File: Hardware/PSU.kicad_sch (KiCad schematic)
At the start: 6 parts, among them J2 Power, U3 HT7533

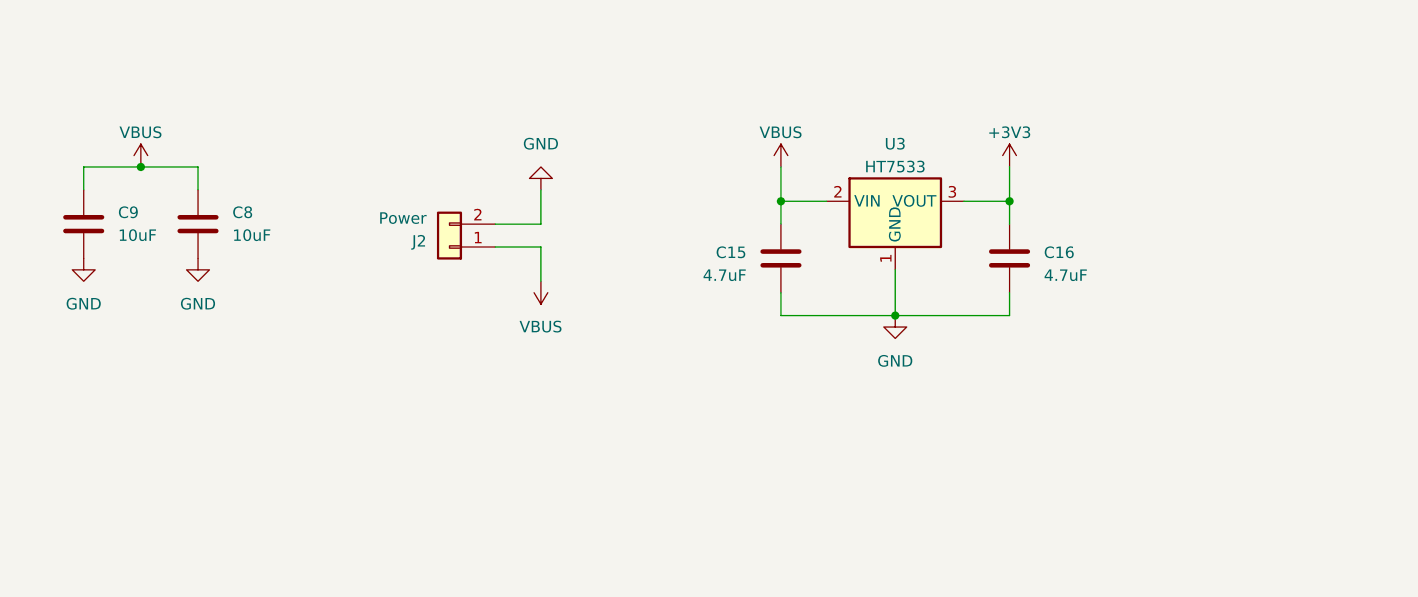
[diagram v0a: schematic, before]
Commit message: 完成原理图设计，完成初步布局布线
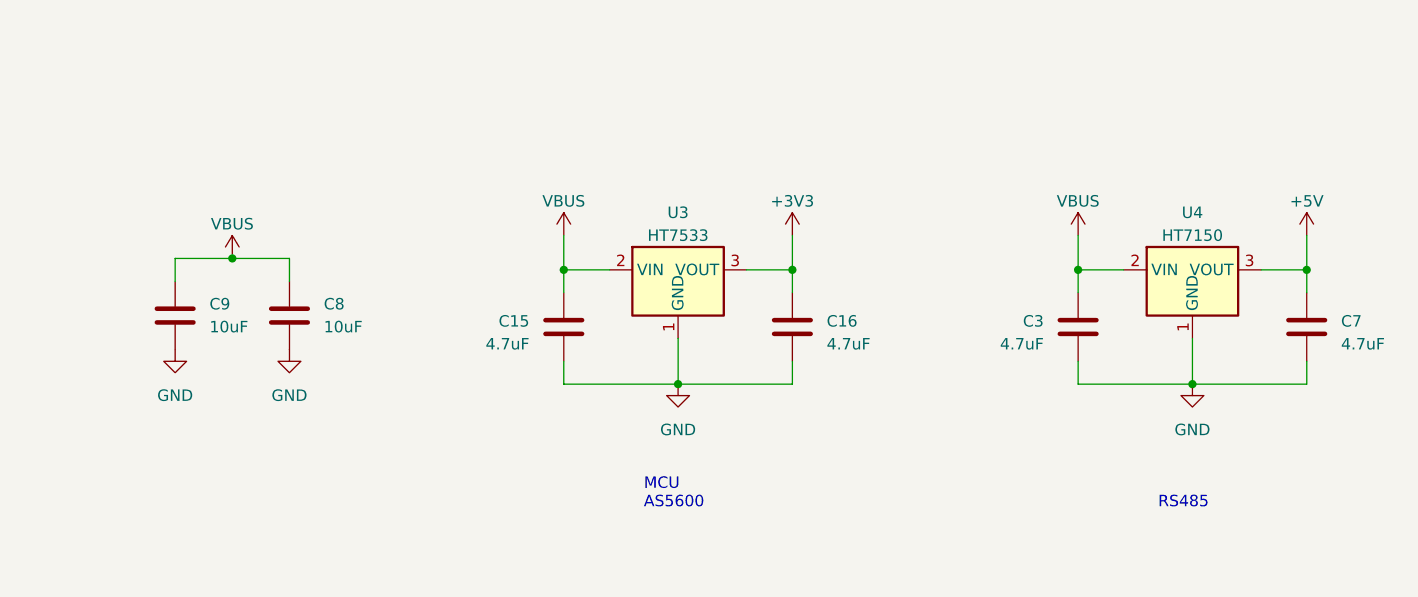
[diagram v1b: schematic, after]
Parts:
- removed J2: Power, Connector_JST:JST_SH_BM02B-SRSS-TB_1x02-1MP_P1.00mm_Vertical, symbol Connector_Generic:Conn_01x02
- added C3, C7: 4.7uF, myDevice:0603_C, symbol Device:C
- added U4: HT7150, Package_TO_SOT_SMD:SOT-89-3, symbol Regulator_Linear:HT75xx-1-SOT89
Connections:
- net GND: now also C3.2, C7.2, U4.1 (GND)
- net VBUS: now also C3.1, U4.2 (VIN)
- new net +5V: C7.1, U4.3 (VOUT)
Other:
- note added: "MCU AS5600"
- note added: "RS485"
- moved on the sheet: C15, C16, C8, C9, U3

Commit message: 基本完成PCB设计
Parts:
- removed C15, C3: 4.7uF, myDevice:0603_C, symbol Device:C
- added C9: 10uF, Capacitor_SMD:C_1206_3216Metric, symbol Device:C
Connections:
- net GND: now also C9.2; no longer C8.2, C9.2
- net VBUS: now also C9.1
- new net GNDPWR: C8.2, C9.2

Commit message: 第一版硬件做好啦！(●'◡'●)
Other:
- company: (none) -> Akako Industry
- title: (none) -> cwFOC/PSU
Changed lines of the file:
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@@
 (kicad_sch (version 20230121) (generator eeschema)
   (paper "A4")
+  (title_block
+    (title "cwFOC/PSU")
+    (date "2023-03-19")
+    (rev "1.0")
+    (company "Akako Industry")
+    (comment 1 "赤紫绮")
+    (comment 2 "赤紫绮")
+    (comment 3 "赤紫绮")
+  )
   (junction (at 93.98 95.25) (diameter 0) (color 0 0 0 0)
   )

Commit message: 小修小补，拉了点线
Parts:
- removed U4: HT7150, Package_TO_SOT_SMD:SOT-89-3, symbol Regulator_Linear:HT75xx-1-SOT89
- added D6: D_TVS, Diode_SMD:D_SMA, symbol Device:D_TVS
- added R19: 0R, myDevice:0603_R, symbol Device:R
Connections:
- net +5V is gone; now on net VBUS: C7.1
- net GND: now also R19.1; no longer C9.2
- net GNDPWR: now also C9.2, D6.2 (A2), R19.2
- net VBUS: now also D6.1 (A1)
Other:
- note added: "AS5600"
- note added: "MCU"
- note removed: "MCU AS5600"
- company: Akako Industry -> Akako Science & Industry

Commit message: 完成第二版硬件
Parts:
- removed C8: 10uF, Capacitor_SMD:C_1206_3216Metric, symbol Device:C
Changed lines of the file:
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@@
-    (stroke (width 0) (type default))
-  )
-  (wire (pts (xy 106.68 97.79) (xy 106.68 95.25))
     (stroke (width 0) (type default))
   )
@@
   )
   (wire (pts (xy 100.33 77.47) (xy 109.22 77.47))
-    (stroke (width 0) (type default))
-  )
-  (wire (pts (xy 93.98 95.25) (xy 106.68 95.25))
     (stroke (width 0) (type default))
   )
@@
     )
   )
-  (symbol (lib_id "power:GNDPWR") (at 106.68 105.41 0) (unit 1)
-    (in_bom yes) (on_board yes) (dnp no) (fields_autoplaced)
-    (property "Reference" "#PWR012" (at 106.68 110.49 0)
-      (effects (font (size 1.27 1.27)) hide)
-    )
-    (property "Value" "GNDPWR" (at 106.553 110.49 0)
-      (effects (font (size 1.27 1.27)))
-    )
-    (property "Footprint" "" (at 106.68 106.68 0)
-      (effects (font (size 1.27 1.27)) hide)
-    )
-    (property "Datasheet" "" (at 106.68 106.68 0)
-      (effects (font (size 1.27 1.27)) hide)
-    )
-    (pin "1")
-    (instances
-      (project "cwFOC"
-        (path "/ff847474-9801-42c6-af12-b4b1b75aa0af/89ac2ee5-3a75-4dad-932f-07f3c050794c"
-          (reference "#PWR012") (unit 1)
-        )
-      )
-    )
-  )
   (symbol (lib_id "power:GNDPWR") (at 81.28 105.41 0) (unit 1)
     (in_bom yes) (on_board yes) (dnp no) (fields_autoplaced)
@@
         )
       )
-    )
-  )
-  (symbol (lib_id "Device:C") (at 106.68 101.6 0) (unit 1)
-    (in_bom yes) (on_board yes) (dnp no) (fields_autoplaced)
-    (property "Reference" "C8" (at 110.49 100.33 0)
-      (effects (font (size 1.27 1.27)) (justify left))
-    )
-    (property "Value" "10uF" (at 110.49 102.87 0)
-      (effects (font (size 1.27 1.27)) (justify left))
-    )
-    (property "Footprint" "Capacitor_SMD:C_1206_3216Metric" (at 107.6452 105.41 0)
-      (effects (font (size 1.27 1.27)) hide)
-    )
-    (property "Datasheet" "~" (at 106.68 101.6 0)
-      (effects (font (size 1.27 1.27)) hide)
-    )
-    (pin "1")
-    (pin "2")
-    (instances
-      (project "cwFOC"
-        (path "/ff847474-9801-42c6-af12-b4b1b75aa0af"
-          (reference "C8") (unit 1)
-        )
-        (path "/ff847474-9801-42c6-af12-b4b1b75aa0af/89ac2ee5-3a75-4dad-932f-07f3c050794c"
-          (reference "C9") (unit 1)
-        )
-      )
